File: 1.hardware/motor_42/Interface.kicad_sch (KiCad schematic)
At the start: 20 parts, among them J8 BOOT_EN, U4 TL431AIDBZR, U5 MT6816CT, U6 ESP32-C3-WROOM-02

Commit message: 얼추 다 그림
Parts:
- removed LED3: LED_0603_Green_PWR, PCM_LED_SMD_AKL:LED_0603_1608Metric, symbol PCM_LED_AKL:LED_0603_Green
- removed R27: 4.7K/0.063w, Resistor_SMD:R_0402_1005Metric, symbol Device:R_Small_US
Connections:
- net at LED4.1 (K): now also U6.7 (IO8); no longer U6.4 (IO5)
- net at LED5.1 (K): now also U6.6 (IO7); no longer U6.3 (IO4)

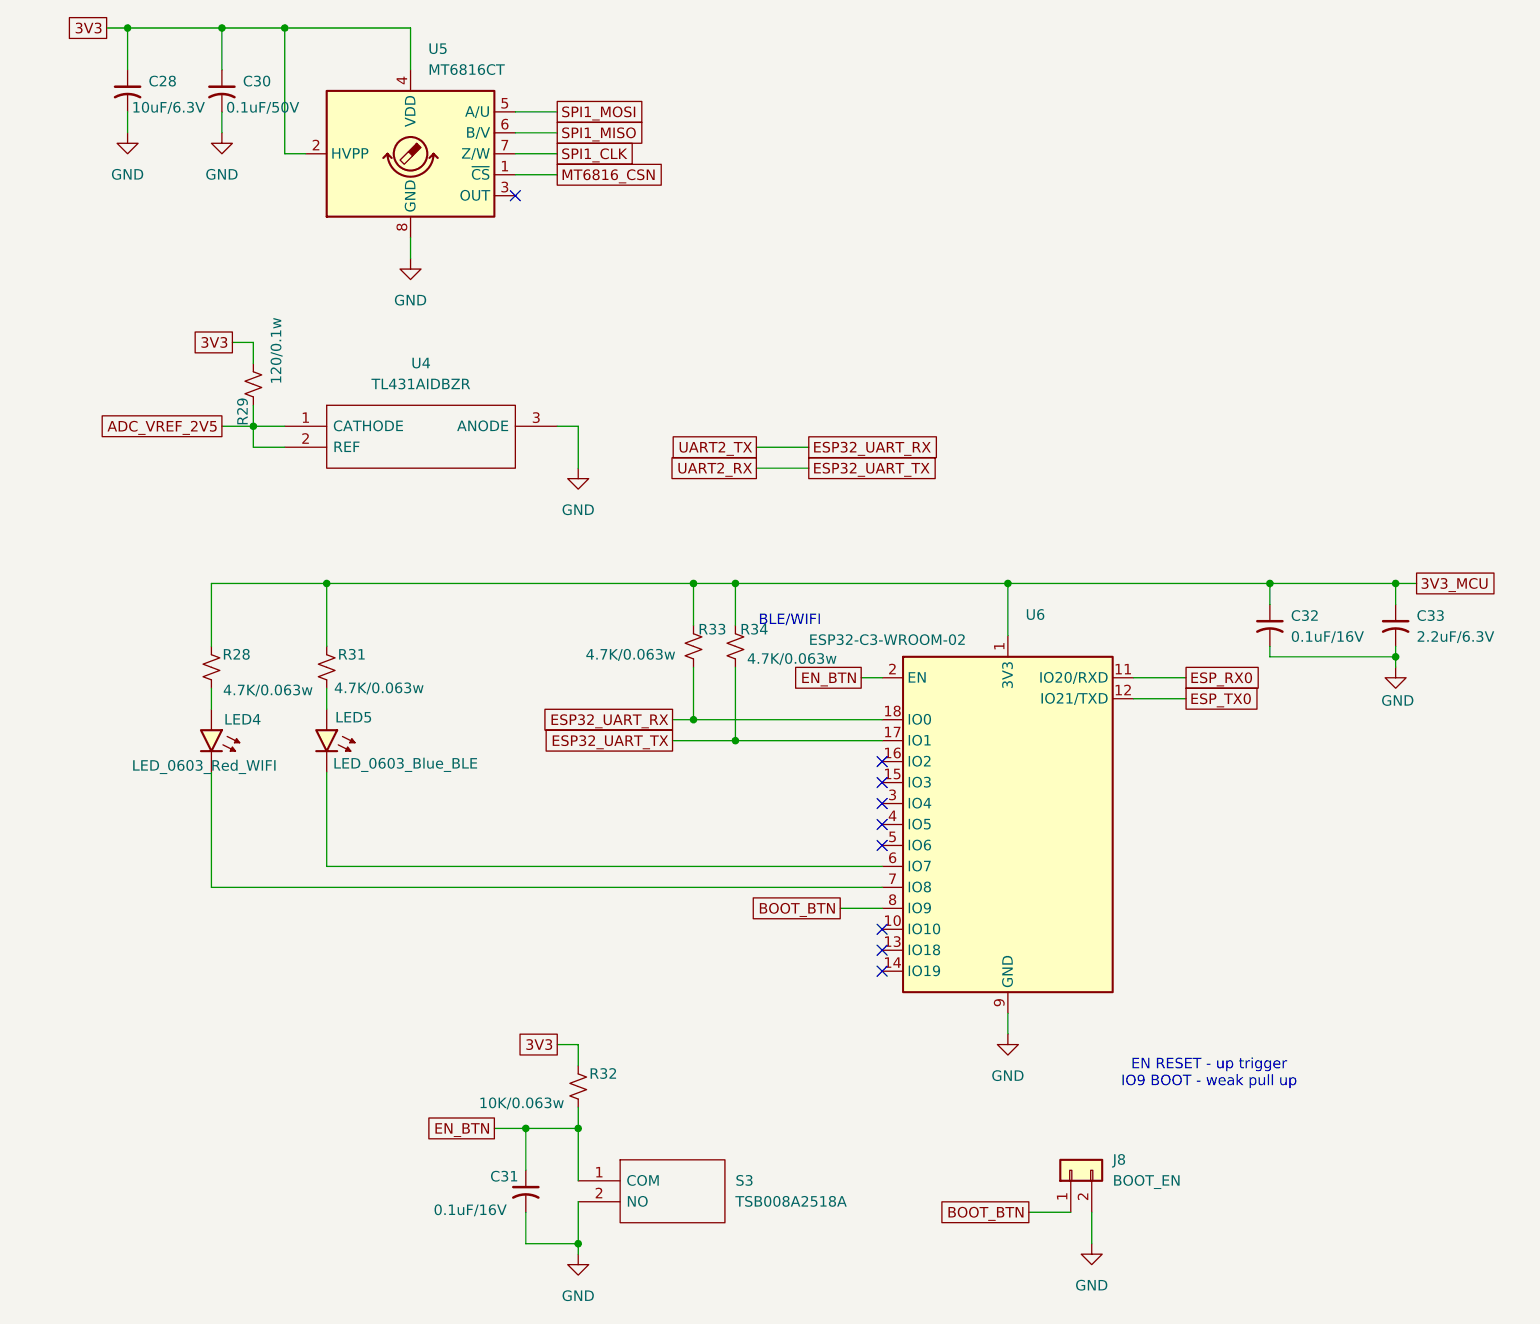
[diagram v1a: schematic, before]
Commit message: 비아 변경 필요
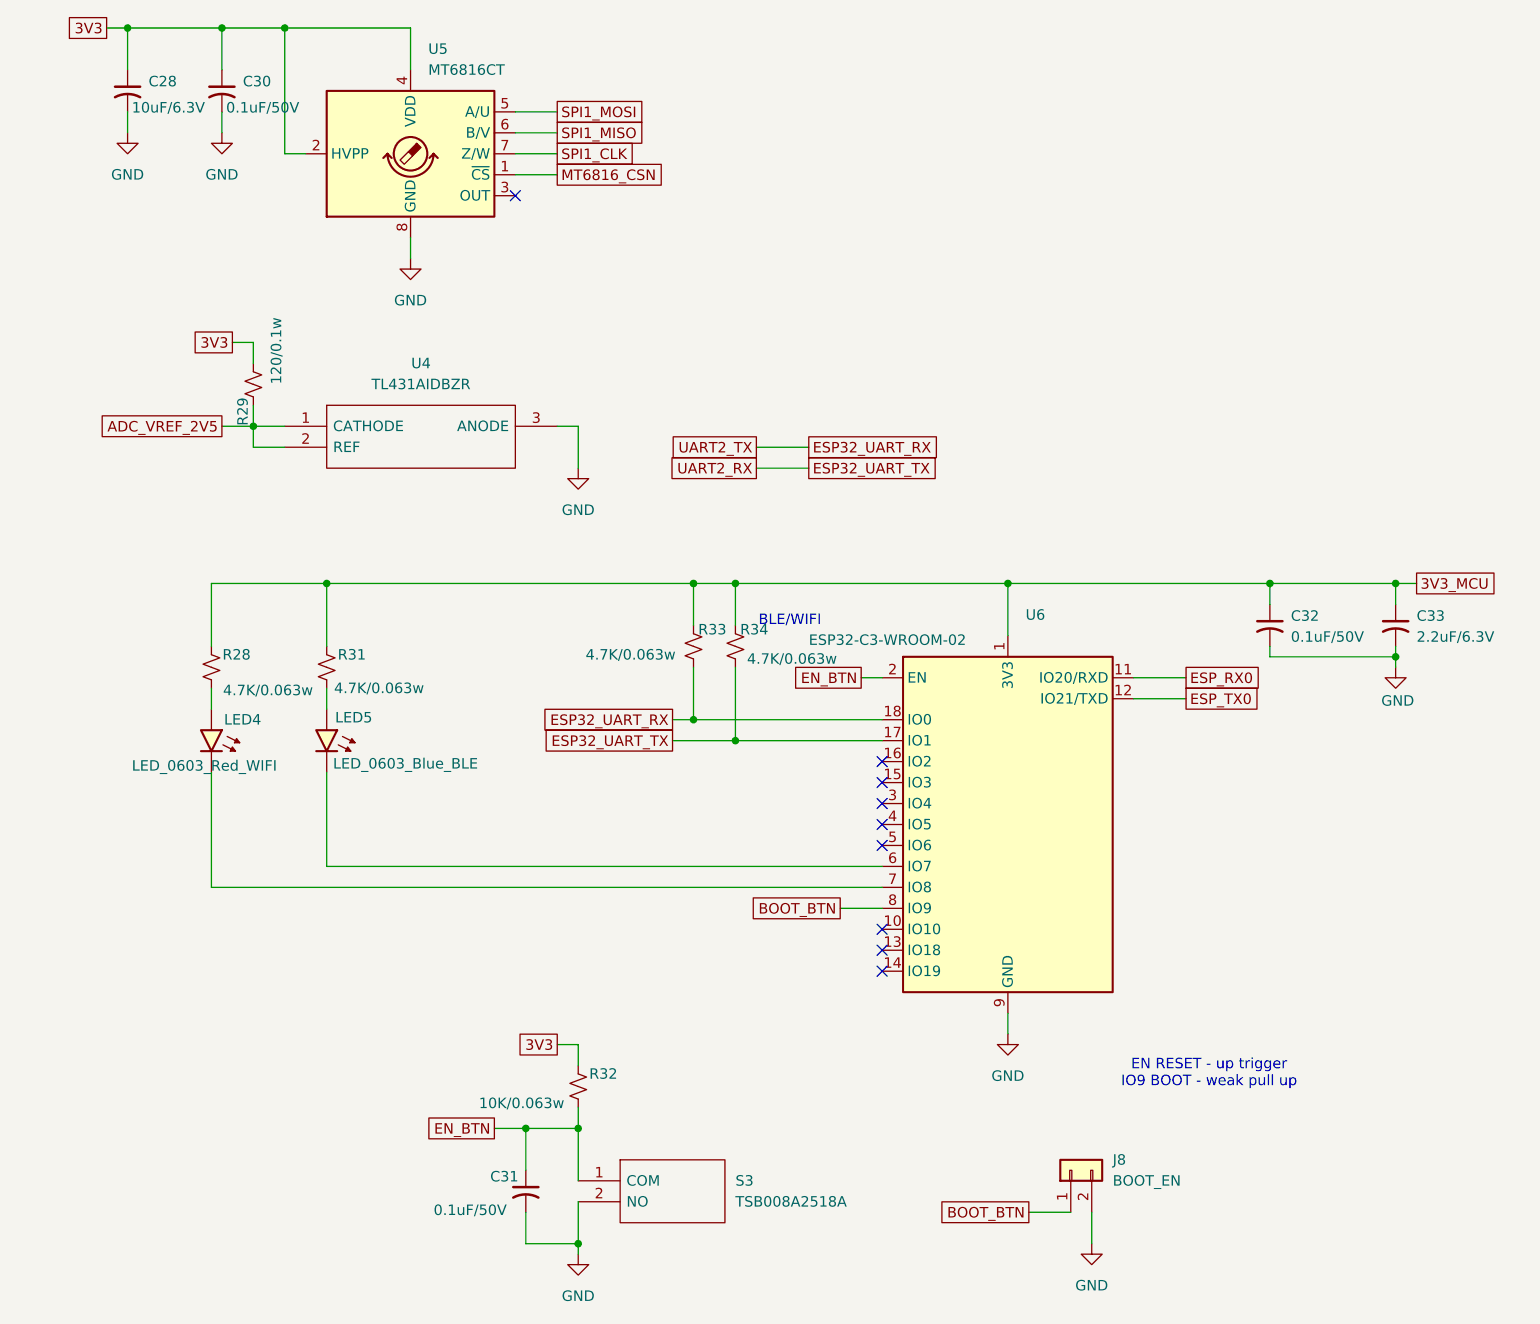
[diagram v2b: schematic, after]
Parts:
- C31, C32: value 0.1uF/16V -> 0.1uF/50V
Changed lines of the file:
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@@
 			)
 		)
-		(property "Value" "0.1uF/16V"
+		(property "Value" "0.1uF/50V"
 			(at 173.99 99.1869 0)
 			(effects
@@
 			)
 		)
-		(property "Value" "0.1uF/16V"
+		(property "Value" "0.1uF/50V"
 			(at 70.104 168.656 0)
 			(effects

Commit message: 번호 초기화 및 led 변경
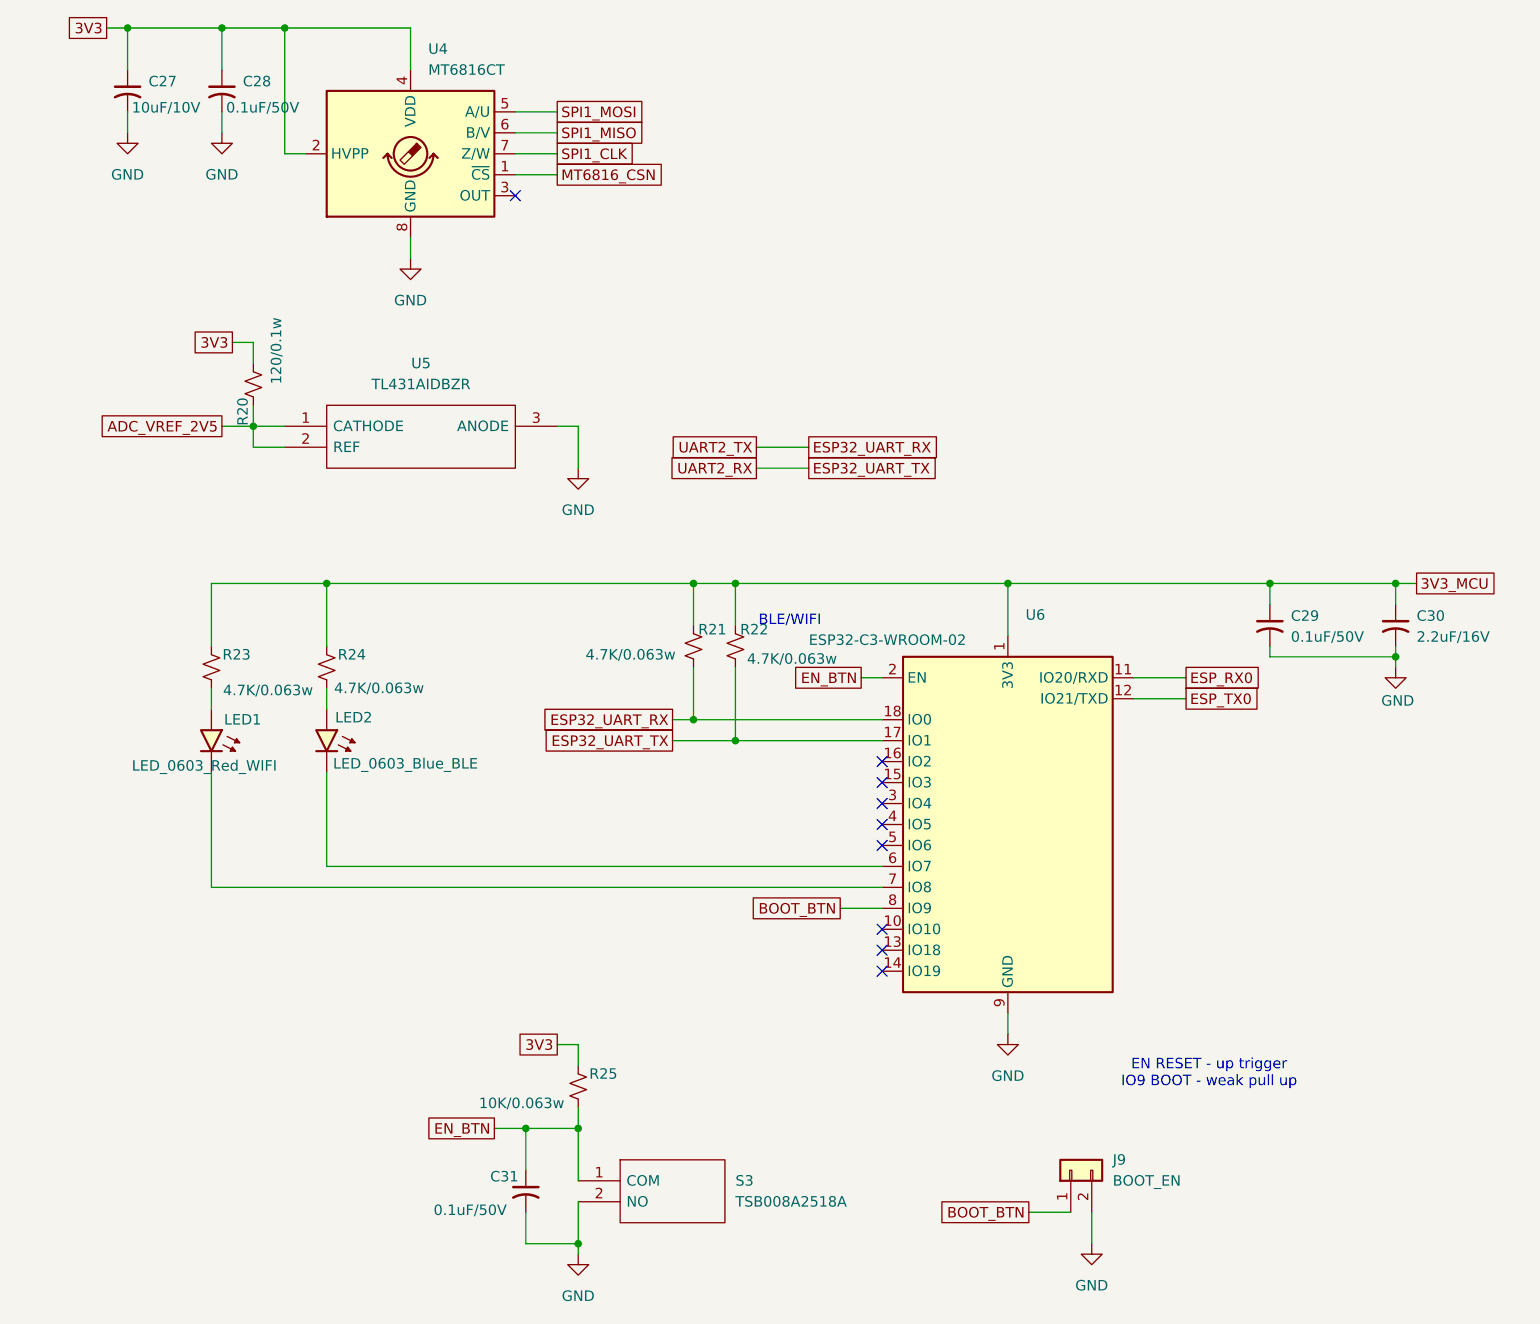
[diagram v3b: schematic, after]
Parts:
- C27: renamed from C28; value 10uF/6.3V -> 10uF/10V
- C30: renamed from C33; value 2.2uF/6.3V -> 2.2uF/16V
- renumbered C30 to C28, C32 to C29, J8 to J9, LED4 to LED1, LED5 to LED2, R29 to R20, R33 to R21, R34 to R22, R28 to R23, R31 to R24, R32 to R25, U5 to U4, U4 to U5
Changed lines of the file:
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@@
 		(on_board yes)
 		(dnp no)
-		(property "Reference" "R32"
+		(property "Reference" "R25"
 			(at 90.678 152.146 0)
 			(effects
@@
 			(project "motor_42"
 				(path "/3c5de6a8-6840-43a5-a2fb-24dbb7f0450d/9b49f0d1-725c-46a9-83d3-f1e791b8bf0d"
-					(reference "R32")
+					(reference "R25")
 					(unit 1)
 				)
@@
 		(on_board yes)
 		(dnp no)
-		(property "Reference" "R31"
+		(property "Reference" "R24"
 			(at 60.198 101.346 0)
 			(effects
@@
 			(project "motor_42"
 				(path "/3c5de6a8-6840-43a5-a2fb-24dbb7f0450d/9b49f0d1-725c-46a9-83d3-f1e791b8bf0d"
-					(reference "R31")
+					(reference "R24")
 					(unit 1)
 				)
@@
 		(dnp no)
 		(fields_autoplaced yes)
-		(property "Reference" "U5"
+		(property "Reference" "U4"
 			(at 69.4533 27.94 0)
 			(effects
@@
 			(project "motor_42"
 				(path "/3c5de6a8-6840-43a5-a2fb-24dbb7f0450d/9b49f0d1-725c-46a9-83d3-f1e791b8bf0d"
-					(reference "U5")
+					(reference "U4")
 					(unit 1)
 				)
@@
 		(dnp no)
 		(fields_autoplaced yes)
-		(property "Reference" "#PWR052"
+		(property "Reference" "#PWR042"
 			(at 87.63 85.09 0)
 			(effects
@@
 			(project "motor_42"
 				(path "/3c5de6a8-6840-43a5-a2fb-24dbb7f0450d/9b49f0d1-725c-46a9-83d3-f1e791b8bf0d"
-					(reference "#PWR052")
+					(reference "#PWR042")
 					(unit 1)
 				)
@@
 		(on_board yes)
 		(dnp no)
-		(property "Reference" "#PWR055"
+		(property "Reference" "#PWR043"
 			(at 186.69 109.22 0)
 			(effects
@@
 			(project "motor_42"
 				(path "/3c5de6a8-6840-43a5-a2fb-24dbb7f0450d/9b49f0d1-725c-46a9-83d3-f1e791b8bf0d"
-					(reference "#PWR055")
+					(reference "#PWR043")
 					(unit 1)
 				)
@@
 		(dnp no)
 		(fields_autoplaced yes)
-		(property "Reference" "U4"
+		(property "Reference" "U5"
 			(at 68.58 66.04 0)
 			(effects
@@
 			(project "motor_42"
 				(path "/3c5de6a8-6840-43a5-a2fb-24dbb7f0450d/9b49f0d1-725c-46a9-83d3-f1e791b8bf0d"
-					(reference "U4")
+					(reference "U5")
 					(unit 1)
 				)
@@
 		(dnp no)
 		(fields_autoplaced yes)
-		(property "Reference" "#PWR050"
+		(property "Reference" "#PWR041"
 			(at 67.31 59.69 0)
 			(effects
@@
 			(project "motor_42"
 				(path "/3c5de6a8-6840-43a5-a2fb-24dbb7f0450d/9b49f0d1-725c-46a9-83d3-f1e791b8bf0d"
-					(reference "#PWR050")
+					(reference "#PWR041")
 					(unit 1)
 				)
@@
 		(dnp no)
 		(fields_autoplaced yes)
-		(property "Reference" "C32"
+		(property "Reference" "C29"
 			(at 173.99 96.6469 0)
 			(effects
@@
 			(project "motor_42"
 				(path "/3c5de6a8-6840-43a5-a2fb-24dbb7f0450d/9b49f0d1-725c-46a9-83d3-f1e791b8bf0d"
-					(reference "C32")
+					(reference "C29")
 					(unit 1)
 				)
@@
 		(dnp no)
 		(fields_autoplaced yes)
-		(property "Reference" "J8"
+		(property "Reference" "J9"
 			(at 152.4 162.5599 90)
 			(effects
@@
 			(project ""
 				(path "/3c5de6a8-6840-43a5-a2fb-24dbb7f0450d/9b49f0d1-725c-46a9-83d3-f1e791b8bf0d"
-					(reference "J8")
+					(reference "J9")
 					(unit 1)
 				)
@@
 		(dnp no)
 		(fields_autoplaced yes)
-		(property "Reference" "#PWR047"
+		(property "Reference" "#PWR039"
 			(at 33.02 44.45 0)
 			(effects
@@
 			(project "motor_42"
 				(path "/3c5de6a8-6840-43a5-a2fb-24dbb7f0450d/9b49f0d1-725c-46a9-83d3-f1e791b8bf0d"
-					(reference "#PWR047")
+					(reference "#PWR039")
 					(unit 1)
 				)
@@
 		(dnp no)
 		(fields_autoplaced yes)
-		(property "Reference" "#PWR053"
+		(property "Reference" "#PWR045"
 			(at 149.86 179.07 0)
 			(effects
@@
 			(project "motor_42"
 				(path "/3c5de6a8-6840-43a5-a2fb-24dbb7f0450d/9b49f0d1-725c-46a9-83d3-f1e791b8bf0d"
-					(reference "#PWR053")
+					(reference "#PWR045")
 					(unit 1)
 				)
@@
 		(on_board yes)
 		(dnp no)
-		(property "Reference" "R28"
+		(property "Reference" "R23"
 			(at 46.228 101.346 0)
 			(effects
@@
 			(project "motor_42"
 				(path "/3c5de6a8-6840-43a5-a2fb-24dbb7f0450d/9b49f0d1-725c-46a9-83d3-f1e791b8bf0d"
-					(reference "R28")
+					(reference "R23")
 					(unit 1)
 				)
@@
 		(on_board yes)
 		(dnp no)
-		(property "Reference" "C28"
+		(property "Reference" "C27"
 			(at 35.56 31.8769 0)
 			(effects
@@
 			)
 		)
-		(property "Value" "10uF/6.3V"
+		(property "Value" "10uF/10V"
 			(at 33.528 35.052 0)
 			(effects
@@
 			(project "motor_42"
 				(path "/3c5de6a8-6840-43a5-a2fb-24dbb7f0450d/9b49f0d1-725c-46a9-83d3-f1e791b8bf0d"
-					(reference "C28")
+					(reference "C27")
 					(unit 1)
 				)
@@
 		(on_board yes)
 		(dnp no)
-		(property "Reference" "LED4"
+		(property "Reference" "LED1"
 			(at 44.704 109.22 90)
 			(effects
@@
 			(project "motor_42"
 				(path "/3c5de6a8-6840-43a5-a2fb-24dbb7f0450d/9b49f0d1-725c-46a9-83d3-f1e791b8bf0d"
-					(reference "LED4")
+					(reference "LED1")
 					(unit 1)
 				)
@@
 		(on_board yes)
 		(dnp no)
-		(property "Reference" "C30"
+		(property "Reference" "C28"
 			(at 46.99 31.8769 0)
 			(effects
@@
 			(project "motor_42"
 				(path "/3c5de6a8-6840-43a5-a2fb-24dbb7f0450d/9b49f0d1-725c-46a9-83d3-f1e791b8bf0d"
-					(reference "C30")
+					(reference "C28")
 					(unit 1)
 				)
@@
 		(on_board yes)
 		(dnp no)
-		(property "Reference" "R34"
+		(property "Reference" "R22"
 			(at 108.966 98.298 0)
 			(effects
@@
 			(project "motor_42"
 				(path "/3c5de6a8-6840-43a5-a2fb-24dbb7f0450d/9b49f0d1-725c-46a9-83d3-f1e791b8bf0d"
-					(reference "R34")
+					(reference "R22")
 					(unit 1)
 				)
@@
 		(dnp no)
 		(fields_autoplaced yes)
-		(property "Reference" "#PWR051"
+		(property "Reference" "#PWR046"
 			(at 87.63 180.34 0)
 			(effects
@@
 			(project "motor_42"
 				(path "/3c5de6a8-6840-43a5-a2fb-24dbb7f0450d/9b49f0d1-725c-46a9-83d3-f1e791b8bf0d"
-					(reference "#PWR051")
+					(reference "#PWR046")
 					(unit 1)
 				)
@@
 		(on_board yes)
 		(dnp no)
-		(property "Reference" "LED5"
+		(property "Reference" "LED2"
 			(at 58.166 108.966 90)
 			(effects
@@
 			(project "motor_42"
 				(path "/3c5de6a8-6840-43a5-a2fb-24dbb7f0450d/9b49f0d1-725c-46a9-83d3-f1e791b8bf0d"
-					(reference "LED5")
+					(reference "LED2")
 					(unit 1)
 				)
@@
 		(on_board yes)
 		(dnp no)
-		(property "Reference" "R33"
+		(property "Reference" "R21"
 			(at 103.886 98.298 0)
 			(effects
@@
 			(project "motor_42"
 				(path "/3c5de6a8-6840-43a5-a2fb-24dbb7f0450d/9b49f0d1-725c-46a9-83d3-f1e791b8bf0d"
-					(reference "R33")
+					(reference "R21")
 					(unit 1)
 				)
@@
 		(dnp no)
 		(fields_autoplaced yes)
-		(property "Reference" "#PWR054"
+		(property "Reference" "#PWR044"
 			(at 139.7 153.67 0)
 			(effects
@@
 			(project "motor_42"
 				(path "/3c5de6a8-6840-43a5-a2fb-24dbb7f0450d/9b49f0d1-725c-46a9-83d3-f1e791b8bf0d"
-					(reference "#PWR054")
+					(reference "#PWR044")
 					(unit 1)
 				)
@@
 		(dnp no)
 		(fields_autoplaced yes)
-		(property "Reference" "C33"
+		(property "Reference" "C30"
 			(at 189.23 96.6469 0)
 			(effects
@@
 			)
 		)
-		(property "Value" "2.2uF/6.3V"
+		(property "Value" "2.2uF/16V"
 			(at 189.23 99.1869 0)
 			(effects
@@
 			(project "motor_42"
 				(path "/3c5de6a8-6840-43a5-a2fb-24dbb7f0450d/9b49f0d1-725c-46a9-83d3-f1e791b8bf0d"
-					(reference "C33")
+					(reference "C30")
 					(unit 1)
 				)
@@
 		(on_board yes)
 		(dnp no)
-		(property "Reference" "R29"
+		(property "Reference" "R20"
 			(at 46.99 71.882 90)
 			(effects
@@
 			(project "motor_42"
 				(path "/3c5de6a8-6840-43a5-a2fb-24dbb7f0450d/9b49f0d1-725c-46a9-83d3-f1e791b8bf0d"
-					(reference "R29")
+					(reference "R20")
 					(unit 1)
 				)
@@
 		(dnp no)
 		(fields_autoplaced yes)
-		(property "Reference" "#PWR048"
+		(property "Reference" "#PWR040"
 			(at 44.45 44.45 0)
 			(effects
@@
 			(project "motor_42"
 				(path "/3c5de6a8-6840-43a5-a2fb-24dbb7f0450d/9b49f0d1-725c-46a9-83d3-f1e791b8bf0d"
-					(reference "#PWR048")
-					(unit 1)
-				)
+					(reference "#PWR040")
+					(unit 1)
+				)
